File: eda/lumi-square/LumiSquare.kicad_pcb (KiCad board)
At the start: 2 copper layers, 166.5 x 100 mm, 57 parts, among them J1 USB_C_Receptacle_USB2.0_14P, J2 Conn_01x04, J3 Conn_01x04, J4 Conn_01x04, J5 Conn_01x04, J5 USB_C_Receptacle_USB2.0, J6 Conn_01x04, J7 Conn_01x04, Q1 IRLML6244, Q3 IRLML2246, Q4 MMBT3904, Q5 MMBT3904, Q6 MMBT3904, Q7 MMBT3904, U1 MCP73831-2-OT, U2 TPS3840, U3 TLV61070A, U3333333 ATSAMD21J18A-A, U4 TLV61070A, U6 STP16CPC05MTR, U8 MIC5225-3.3YM5

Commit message: - uploading kicad pcb changes
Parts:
- removed J4, J7: Conn_01x04, Connector_PinSocket_2.54mm:PinSocket_1x04_P2.54mm_Vertical
- removed U$1: LOGO-SFE, Button_Pad_Breakout-v05:SFE-NEW-WEBLOGO
- added C11: .001uF, Capacitor_SMD:C_0603_1608Metric_Pad1.08x0.95mm_HandSolder, F.Cu at (175.6, 62.4)
- added C12: .01uF, Capacitor_SMD:C_0603_1608Metric_Pad1.08x0.95mm_HandSolder, F.Cu at (175.6, 64.9)
- added C13: 1uF, Capacitor_THT:CP_Radial_D6.3mm_P2.50mm, F.Cu at (162.6, 65.1)
- added C14: 1uF, Capacitor_THT:CP_Radial_D6.3mm_P2.50mm, F.Cu at (162.6, 73.0)
- added C15: 1uF, Capacitor_THT:CP_Radial_D6.3mm_P2.50mm, F.Cu at (162.6, 80.8)
- added C16: .1uF, Capacitor_SMD:C_1206_3216Metric, F.Cu at (170.6, 62.9)
- added C17: .1uF, Capacitor_SMD:C_1206_3216Metric, F.Cu at (170.6, 66.2)
- added C18: .1uF, Capacitor_SMD:C_1206_3216Metric, F.Cu at (170.6, 69.5)
- added C19: .1uF, Capacitor_SMD:C_1206_3216Metric, F.Cu at (170.6, 72.9)
- added C20: .1uF, Capacitor_SMD:C_1206_3216Metric, F.Cu at (170.6, 76.2)
- added C21: .1uF, Capacitor_SMD:C_1206_3216Metric, F.Cu at (170.6, 79.6)
- added D4: 1N4148W, Diode_SMD:D_SOD-123, F.Cu at (180.7, 62.9)
- added Q2: IRLML2246, Package_TO_SOT_SMD:SOT-23, F.Cu at (156.4, 95.2)
- added Q8: MMBT3904, Package_TO_SOT_SMD:SOT-23, F.Cu at (180.2, 66.8)
- added R11: 220k, Resistor_SMD:R_0603_1608Metric_Pad0.98x0.95mm_HandSolder, F.Cu at (156.1, 98.7)
- added R12: 1k, Resistor_SMD:R_0603_1608Metric_Pad0.98x0.95mm_HandSolder, F.Cu at (175.6, 67.5)
- added R14: 15k, Resistor_SMD:R_0603_1608Metric_Pad0.98x0.95mm_HandSolder, F.Cu at (175.6, 70.0)
- added R15: 15k, Resistor_SMD:R_0603_1608Metric_Pad0.98x0.95mm_HandSolder, F.Cu at (175.6, 72.5)
- added R20: 15k, Resistor_SMD:R_0603_1608Metric_Pad0.98x0.95mm_HandSolder, F.Cu at (175.6, 75.0)
- added R21: 10k, Resistor_SMD:R_0603_1608Metric_Pad0.98x0.95mm_HandSolder, F.Cu at (175.6, 77.5)
- added R22: 2.2k, Resistor_SMD:R_0603_1608Metric_Pad0.98x0.95mm_HandSolder, F.Cu at (175.6, 80.0)
- BT1: moved to B.Cu
- J2, J3: value Conn_01x04 -> Conn_01x12; footprint Connector_PinSocket_2.54mm:PinSocket_1x04_P2.54mm_Vertical -> Connector_PinSocket_2.54mm:PinSocket_1x12_P2.54mm_Vertical
- J5, J6: value Conn_01x04 -> Conn_01x08; footprint Connector_PinSocket_2.54mm:PinSocket_1x04_P2.54mm_Vertical -> Connector_PinSocket_2.54mm:PinSocket_1x08_P2.54mm_Vertical
- R13: value 10k -> 100k
- moved C1 120.6 mm to (164.2, 89.5)
- moved C2 120.6 mm to (164.2, 92.0)
- moved C23234545 120.6 mm to (168.5, 89.5)
- moved C3 120.6 mm to (164.2, 94.5)
- moved C3245345 120.6 mm to (164.2, 104.5)
- moved R1 120.6 mm to (168.5, 92.0)
- moved R11 120.6 mm to (172.8, 94.5)
- moved R12 120.6 mm to (172.8, 97.0)
- moved R13 120.6 mm to (172.8, 99.5)
- moved R2 120.6 mm to (168.5, 94.5)
- moved R3 120.6 mm to (168.5, 97.0)
- moved R4 120.6 mm to (168.5, 99.5)
- moved R5 120.6 mm to (168.5, 102.0)
- moved R6 120.6 mm to (168.5, 104.5)
- moved J5 104.4 mm to (249.5, 116.0)
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- renumbered U3333333 to U5
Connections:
- C3 pad 1: /4.2V Bat -> Net-(Q2-D)
- C4 pad 2: /4.2V Bat -> Net-(Q2-D)
- J2 pad 1: /Matrix Switch 1 -> Net-(J2-Pin_1)
- J3 pad 1: /Matrix Switch 2 -> /Row/Input 1
- J3 pad 2: Net-(J3-Pin_2) -> /Row/Input 2
- J3 pad 3: Net-(J3-Pin_3) -> /Row/Input 3
- J3 pad 4: Net-(J3-Pin_4) -> /Row/Input 4
- J5 pad 1: /Matrix Switch 4 -> +3.3V Main
- J5 pad 2: Net-(J5-Pin_2) -> /MCU TX
- J5 pad 3: Net-(J5-Pin_3) -> /MCU RX
- J5 pad 4: Net-(J5-Pin_4) -> unconnected-(J5-Pin_4-Pad4)
- J6 pad 1: Net-(J6-Pin_1) -> unconnected-(J6-Pin_1-Pad1)
- J6 pad 3: Net-(J6-Pin_3) -> unconnected-(J6-Pin_3-Pad3)
- L1 pad 1: /4.2V Bat -> Net-(Q2-D)
- Q4 pad 2: Net-(J6-Pin_1) -> Net-(J3-Pin_9)
- Q5 pad 2: Net-(J6-Pin_3) -> Net-(J3-Pin_10)
- Q6 pad 2: Net-(J7-Pin_1) -> Net-(J3-Pin_11)
- Q7 pad 2: Net-(J7-Pin_3) -> Net-(J3-Pin_12)
- R16 pad 1: unconnected-(R16-Pad1) -> /LED Col 1
- R17 pad 1: unconnected-(R17-Pad1) -> /LED Col 2
- R18 pad 1: unconnected-(R18-Pad1) -> /LED Col 3
- R19 pad 1: unconnected-(R19-Pad1) -> /LED Col 4
- R6 pad 1: /4.2V Bat -> Net-(Q2-D)
- U2 pad 2: /4.2V Bat -> Net-(Q2-D)
- U3 pad 6: /4.2V Bat -> Net-(Q2-D)
- U5 pad 10: unconnected-(U3333333-PB07-Pad10) -> /Col/Output 4
- U5 pad 11: /Matrix Switch 1 -> /Row/Input 1
- U5 pad 12: /Matrix Switch 2 -> /Row/Input 2
- U5 pad 21: unconnected-(U3333333-VDDIO-Pad21) -> +3.3V Main
- U5 pad 22: Net-(U3333333-GND-Pad22) -> GNDREF
- U5 pad 23: /Matrix Switch 3 -> /Row/Input 3
- U5 pad 24: /Matrix Switch 4 -> /Row/Input 4
- U5 pad 25: unconnected-(U3333333-PB12-Pad25) -> /SPI Dout
- U5 pad 26: unconnected-(U3333333-PB13-Pad26) -> /SPI CLK
- U5 pad 27: unconnected-(U3333333-PB14-Pad27) -> /SPI Latch
- U5 pad 33: Net-(U3333333-GND-Pad22) -> GNDREF
- U5 pad 34: unconnected-(U3333333-VDDIO-Pad34) -> +3.3V Main
- U5 pad 39: unconnected-(U3333333-PB16-Pad39) -> /Previous Btn
- U5 pad 40: unconnected-(U3333333-PB17-Pad40) -> /Next Btn
- U5 pad 41: unconnected-(U3333333-PA20-Pad41) -> /MCU TX
- U5 pad 42: unconnected-(U3333333-PA21-Pad42) -> /MCU RX
- U5 pad 47: Net-(U3333333-GND-Pad22) -> GNDREF
- U5 pad 48: unconnected-(U3333333-VDDIO-Pad48) -> +3.3V Main
- U5 pad 49: unconnected-(U3333333-PB22-Pad49) -> /Difficulty Btn
- U5 pad 5: unconnected-(U3333333-PB04-Pad5) -> /Col/Output 1
- U5 pad 50: unconnected-(U3333333-PB23-Pad50) -> /Buzzer PWM
- U5 pad 52: unconnected-(U3333333-~{RESET}-Pad52) -> /Reset Pin
- U5 pad 54: Net-(U3333333-GND-Pad22) -> GNDREF
- U5 pad 55: unconnected-(U3333333-VDDCORE-Pad55) -> /VDD CORE
- U5 pad 56: unconnected-(U3333333-VDDIN-Pad56) -> +3.3V Main
- U5 pad 57: unconnected-(U3333333-PA30-Pad57) -> /SWCLK
- U5 pad 58: unconnected-(U3333333-PA31-Pad58) -> /SWDIO
- U5 pad 6: unconnected-(U3333333-PB05-Pad6) -> /Col/Output 2
- U5 pad 61: unconnected-(U3333333-PB00-Pad61) -> /LED Col 1
- U5 pad 62: unconnected-(U3333333-PB01-Pad62) -> /LED Col 2
- U5 pad 63: unconnected-(U3333333-PB02-Pad63) -> /LED Col 3
- U5 pad 64: unconnected-(U3333333-PB03-Pad64) -> /LED Col 4
- U5 pad 7: unconnected-(U3333333-GNDANA-Pad7) -> GNDREF
- U5 pad 8: unconnected-(U3333333-VDDANA-Pad8) -> +3.3V Main
- U5 pad 9: unconnected-(U3333333-PB06-Pad9) -> /Col/Output 3
- U6 pad 10: Net-(J3-Pin_4) -> Net-(J2-Pin_6)
- U6 pad 11: Net-(J4-Pin_2) -> Net-(J2-Pin_7)
- U6 pad 12: Net-(J4-Pin_3) -> Net-(J2-Pin_8)
- U6 pad 13: Net-(J4-Pin_4) -> Net-(J2-Pin_9)
- U6 pad 14: Net-(J5-Pin_2) -> Net-(J2-Pin_10)
- U6 pad 15: Net-(J5-Pin_3) -> Net-(J2-Pin_11)
- U6 pad 16: Net-(J5-Pin_4) -> Net-(J2-Pin_12)
- U6 pad 2: unconnected-(U6-SIN-Pad2) -> /SPI Dout
- U6 pad 21: unconnected-(U6-BLANK-Pad21) -> GNDREF
- U6 pad 23: unconnected-(U6-RSET-Pad23) -> Net-(U6-RSET)
- U6 pad 3: unconnected-(U6-CLK-Pad3) -> /SPI CLK
- U6 pad 4: unconnected-(U6-LATCH-Pad4) -> /SPI Latch
- U6 pad 5: Net-(J2-Pin_2) -> Net-(J2-Pin_1)
- U6 pad 6: Net-(J2-Pin_3) -> Net-(J2-Pin_2)
- U6 pad 7: Net-(J2-Pin_4) -> Net-(J2-Pin_3)
- U6 pad 8: Net-(J3-Pin_2) -> Net-(J2-Pin_4)
- U6 pad 9: Net-(J3-Pin_3) -> Net-(J2-Pin_5)
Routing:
- net /5V USB: track 16.1 -> 6.01 mm
- net unconnected-(J1-SHIELD-PadS1): track 0.00 -> 10.1 mm
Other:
- board size 166.5 x 100 mm -> 87.2 x 87.2 mm

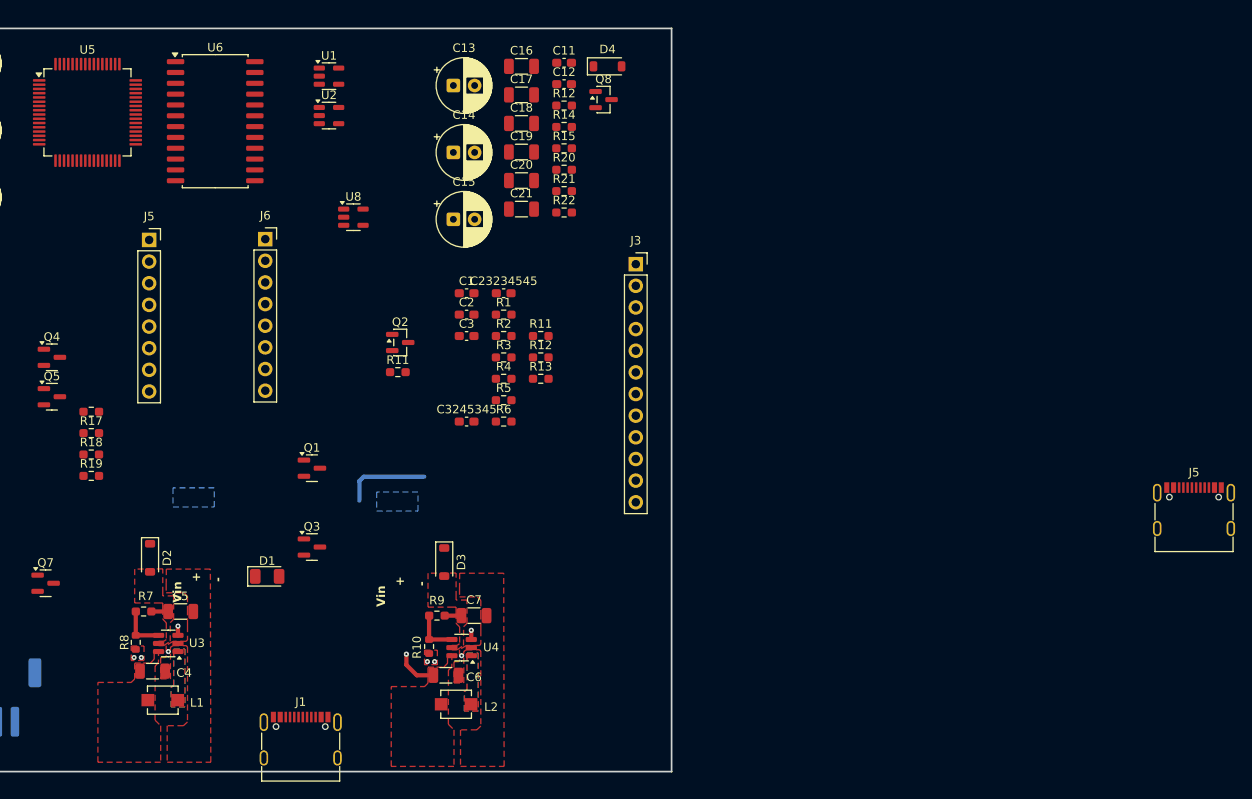
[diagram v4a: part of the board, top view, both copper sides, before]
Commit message: -Added circuity for esd on usb. - Add p chanel mosfets. - added new footprint, symbol, and step files
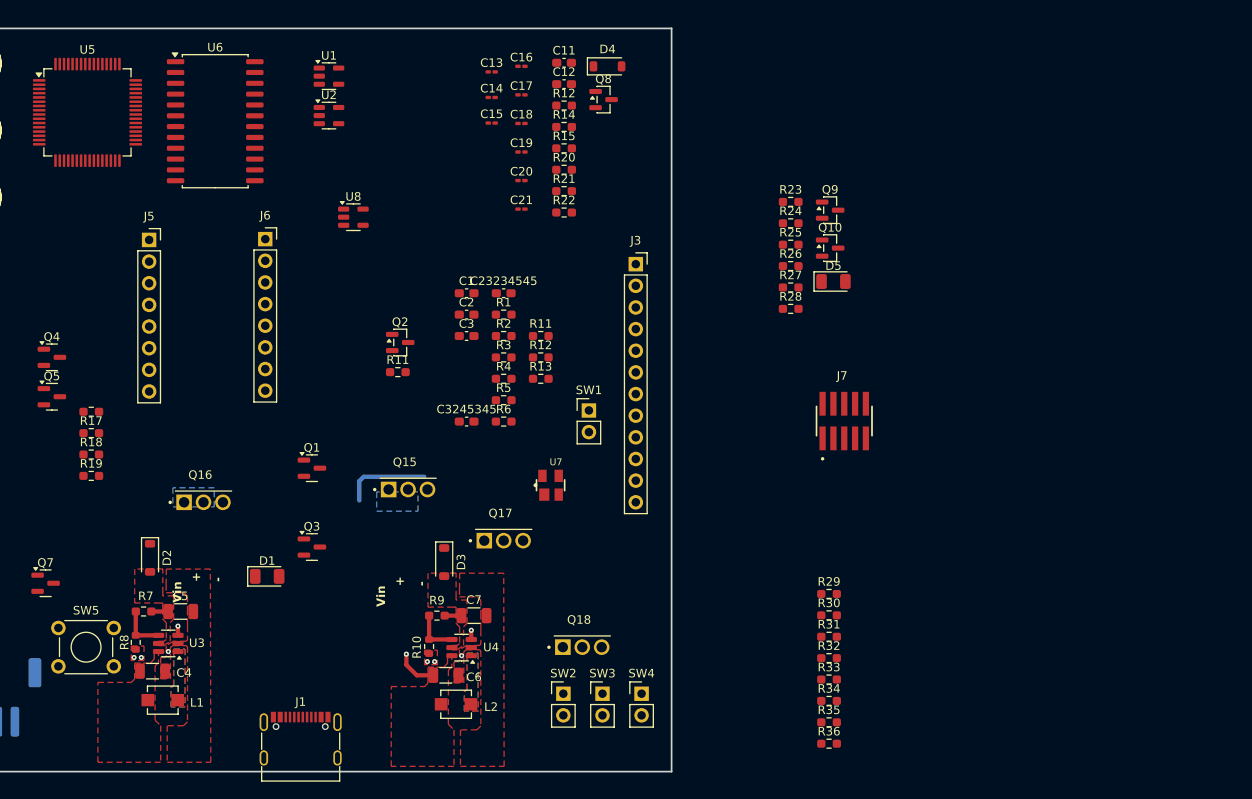
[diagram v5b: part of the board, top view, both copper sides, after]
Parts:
- removed the J5 at (249.5, 116.0)
- added D5: LED, LED_SMD:LED_1206_3216Metric, F.Cu at (207.2, 88.1)
- added J7: FTSH-105-01-X-DV-P-K-X, FTSH-105-01-X-DV-P-K-X:SAMTEC_FTSH-105-01-X-DV-P-K-X, F.Cu at (208.5, 104.5)
- added Q10: IRLML2246, Package_TO_SOT_SMD:SOT-23, F.Cu at (206.8, 84.2)
- added Q15: TSM680P06CH, TSM680P06CH:TO228P680X245X847-3, F.Cu at (157.3, 112.5)
- added Q16: TSM680P06CH, TSM680P06CH:TO228P680X245X847-3, F.Cu at (133.3, 114.0)
- added Q17: TSM680P06CH, TSM680P06CH:TO228P680X245X847-3, F.Cu at (168.5, 118.5)
- added Q18: TSM680P06CH, TSM680P06CH:TO228P680X245X847-3, F.Cu at (177.7, 131.0)
- added Q9: MMBT3904, Package_TO_SOT_SMD:SOT-23, F.Cu at (206.8, 79.7)
- added R23: 330, Resistor_SMD:R_0603_1608Metric_Pad0.98x0.95mm_HandSolder, F.Cu at (202.2, 78.8)
- added R24: 1.3k, Resistor_SMD:R_0603_1608Metric_Pad0.98x0.95mm_HandSolder, F.Cu at (202.2, 81.3)
- added R25: 1.3k, Resistor_SMD:R_0603_1608Metric_Pad0.98x0.95mm_HandSolder, F.Cu at (202.2, 83.8)
- added R26: 33k, Resistor_SMD:R_0603_1608Metric_Pad0.98x0.95mm_HandSolder, F.Cu at (202.2, 86.3)
- added R27: 41k, Resistor_SMD:R_0603_1608Metric_Pad0.98x0.95mm_HandSolder, F.Cu at (202.2, 88.8)
- added R28: 100k, Resistor_SMD:R_0603_1608Metric_Pad0.98x0.95mm_HandSolder, F.Cu at (202.2, 91.3)
- added R29: 100k, Resistor_SMD:R_0603_1608Metric_Pad0.98x0.95mm_HandSolder, F.Cu at (206.7, 124.8)
- added R30: 47k, Resistor_SMD:R_0603_1608Metric_Pad0.98x0.95mm_HandSolder, F.Cu at (206.7, 127.3)
- added R31: 100k, Resistor_SMD:R_0603_1608Metric_Pad0.98x0.95mm_HandSolder, F.Cu at (206.7, 129.8)
- added R32: 47k, Resistor_SMD:R_0603_1608Metric_Pad0.98x0.95mm_HandSolder, F.Cu at (206.7, 132.3)
- added R33: 100k, Resistor_SMD:R_0603_1608Metric_Pad0.98x0.95mm_HandSolder, F.Cu at (206.7, 134.8)
- added R34: 47k, Resistor_SMD:R_0603_1608Metric_Pad0.98x0.95mm_HandSolder, F.Cu at (206.7, 137.3)
- added R35: 100k, Resistor_SMD:R_0603_1608Metric_Pad0.98x0.95mm_HandSolder, F.Cu at (206.7, 139.8)
- added R36: 47k, Resistor_SMD:R_0603_1608Metric_Pad0.98x0.95mm_HandSolder, F.Cu at (206.7, 142.3)
- added SW1: SW_SPST, Connector_PinHeader_2.54mm:PinHeader_1x02_P2.54mm_Vertical, F.Cu at (178.5, 103.2)
- added SW2: SW_Push, Connector_PinHeader_2.54mm:PinHeader_1x02_P2.54mm_Vertical, F.Cu at (175.5, 136.5)
- added SW3: SW_Push, Connector_PinHeader_2.54mm:PinHeader_1x02_P2.54mm_Vertical, F.Cu at (180.1, 136.5)
- added SW4: SW_Push, Connector_PinHeader_2.54mm:PinHeader_1x02_P2.54mm_Vertical, F.Cu at (184.7, 136.5)
- added SW5: SW_Push, Button_Switch_THT:SW_TH_Tactile_Omron_B3F-100x, F.Cu at (116.2, 128.8)
- added U7: CM1224-02SR, CM1224-02SR:SOT143, F.Cu at (174.0, 112.0)
- C13, C14, C15: footprint Capacitor_THT:CP_Radial_D6.3mm_P2.50mm -> Capacitor_SMD:C_0201_0603Metric_Pad0.64x0.40mm_HandSolder
- C16, C17, C18, C19, C20, C21: footprint Capacitor_SMD:C_1206_3216Metric -> Capacitor_SMD:C_0201_0603Metric_Pad0.64x0.40mm_HandSolder
- R12: value 1k -> 200
- moved C15 12.2 mm to (167.1, 69.5)
- moved C14 7.86 mm to (167.1, 66.5)
- moved C13 4.78 mm to (167.1, 63.5)
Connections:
- J1 pad A6: unconnected-(J1-D+-PadA6) -> /TARGET USB P
- J1 pad A7: unconnected-(J1-D--PadA7) -> /TARGET USB N
- J1 pad B6: unconnected-(J1-D+-PadB6) -> /TARGET USB P
- J1 pad B7: unconnected-(J1-D--PadB7) -> /TARGET USB N
- J3 pad 10: Net-(J3-Pin_10) -> /Col 2 Anode
- J3 pad 11: Net-(J3-Pin_11) -> /Col 3 Anode
- J3 pad 12: Net-(J3-Pin_12) -> /Col 4 Anode
- J3 pad 9: Net-(J3-Pin_9) -> /Col 1 Anode
- Q4 pad 2: Net-(J3-Pin_9) -> GNDREF
- Q4 pad 3: /5.3V Out -> Net-(Q4-C)
- Q5 pad 2: Net-(J3-Pin_10) -> GNDREF
- Q5 pad 3: /5.3V Out -> Net-(Q5-C)
- Q6 pad 2: Net-(J3-Pin_11) -> GNDREF
- Q6 pad 3: /5.3V Out -> Net-(Q6-C)
- Q7 pad 2: Net-(J3-Pin_12) -> GNDREF
- Q7 pad 3: /5.3V Out -> Net-(Q7-C)
- U5 pad 31: unconnected-(U5-PA14-Pad31) -> /PA14 USB VBUS
- U5 pad 45: unconnected-(U5-PA24-Pad45) -> /TARGET USB N
- U5 pad 46: unconnected-(U5-PA25-Pad46) -> /TARGET USB P

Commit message: Adding updateds to pcb and schematic design
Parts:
- removed J5, J6: Conn_01x08, Connector_PinSocket_2.54mm:PinSocket_1x08_P2.54mm_Vertical
- removed the R11 at (172.8, 94.5)
- added BZ2: RDT-4.000-1375-NS1, RDT.pretty:RDT-4.000-1375-NS1, F.Cu at (111.0, 135.5)
- added U9: DFR0299, DFR0299:MODULE_DFR0299, F.Cu at (116.5, 70.5)
- C13, C14, C15, C16, C17, C18, C19, C20, C21: footprint Capacitor_SMD:C_0201_0603Metric_Pad0.64x0.40mm_HandSolder -> Capacitor_SMD:C_0603_1608Metric_Pad1.08x0.95mm_HandSolder
- SW5, U6: moved to B.Cu
- moved C1 85.5 mm to (249.6, 86.5)
- moved C23234545 85.5 mm to (253.9, 86.5)
- moved C3245345 85.5 mm to (249.6, 101.5)
- moved R1 85.5 mm to (253.9, 89.0)
- moved R12 85.5 mm to (258.3, 94.0)
- moved R13 85.5 mm to (258.3, 96.5)
- moved R2 85.5 mm to (253.9, 91.5)
- moved R3 85.5 mm to (253.9, 94.0)
- moved R4 85.5 mm to (253.9, 96.5)
- moved J7 75.6 mm to (144.6, 64.0)
- moved R30 74.0 mm to (146.3, 84.5), turned to 180 degrees
- moved R34 72.3 mm to (146.3, 97.5), turned to 180 degrees
- moved C10 72.2 mm to (168.5, 112.5)
- moved D1 70.3 mm to (71.2, 112.0)
- moved C9 69.9 mm to (160.8, 112.5)
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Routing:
- net /Col 1 Anode: track 0.00 -> 56.1 mm
- net /Col 3 Anode: track 0.00 -> 47.9 mm
- net /Col 2 Anode: track 0.00 -> 34.2 mm
- net /5V USB: track 6.01 -> 33.3 mm, vias 2 -> 4
- net /Col 4 Anode: track 0.00 -> 26.5 mm
- net GNDREF: track 0.00 -> 24.0 mm, vias 6 -> 23
- net unconnected-(J1-SHIELD-PadS1): track 10.1 -> 0.00 mm
- net Net-(Q7-B): track 0.00 -> 8.21 mm
- net Net-(Q5-B): track 0.00 -> 8.21 mm
- net Net-(Q6-B): track 0.00 -> 7.87 mm
- net Net-(Q4-B): track 0.00 -> 7.87 mm
- net Net-(Q6-C): track 0.00 -> 7.28 mm
- net Net-(Q7-C): track 0.00 -> 7.06 mm
- net Net-(Q4-C): track 0.00 -> 6.75 mm
- net Net-(Q5-C): track 0.00 -> 6.56 mm
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- added copper zone on F.Cu, net /5.3V Out
- added copper zone on F.Cu, net Net-(Q2-D)
- added copper zone on B.Cu, net Net-(U3-SW)
- added copper zone on F.Cu, net Net-(U3-SW)
- added copper zone on B.Cu, net Net-(U4-SW)
- added copper zone on F.Cu, net Net-(U4-SW)
- removed copper zone on B.Cu, net (none)
- removed copper zone on F.Cu, net (none)
- removed copper zone on F.Cu, net /4.2V Bat
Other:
- board text removed: "+"
- board text removed: "-"
- board text removed: "Vin"

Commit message: Made more progress with the pcb layout
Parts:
- removed C23234545: 1uF, Capacitor_SMD:C_0603_1608Metric_Pad1.08x0.95mm_HandSolder
- removed C3245345: 2.2uF, Capacitor_SMD:C_0603_1608Metric_Pad1.08x0.95mm_HandSolder
- removed the R12 at (258.3, 94.0)
- added C22: 1uF, Capacitor_SMD:C_0603_1608Metric_Pad1.08x0.95mm_HandSolder, F.Cu at (169.5, 73.1)
- added C23: 2.2uF, Capacitor_SMD:C_0603_1608Metric_Pad1.08x0.95mm_HandSolder, F.Cu at (159.5, 73.1)
- added J4: Conn_01x02, Connector_JST:JST_SH_BM02B-SRSS-TB_1x02-1MP_P1.00mm_Vertical, F.Cu at (88.3, 66.7)
- added REF**: M2, MountingHole:MountingHole_2.2mm_M2_DIN965_Pad, F.Cu at (104.5, 142.1)
- added REF**: M2, MountingHole:MountingHole_2.2mm_M2_DIN965_Pad, F.Cu at (104.5, 61.9)
- added REF**: M2, MountingHole:MountingHole_2.2mm_M2_DIN965_Pad, F.Cu at (185.0, 61.6)
- added REF**: M2, MountingHole:MountingHole_2.2mm_M2_DIN965_Pad, F.Cu at (185.0, 142.4)
- C16, C17, C18, C19, C2, C20, U5: moved to B.Cu
- D1, D5: footprint LED_SMD:LED_1206_3216Metric -> Connector_JST:JST_SH_BM02B-SRSS-TB_1x02-1MP_P1.00mm_Vertical
- SW1, SW2, SW3, SW4: footprint Connector_PinHeader_2.54mm:PinHeader_1x02_P2.54mm_Vertical -> Connector_JST:JST_SH_BM02B-SRSS-TB_1x02-1MP_P1.00mm_Vertical
- SW5: footprint Button_Switch_THT:SW_TH_Tactile_Omron_B3F-100x -> Button_Switch_SMD:SW_SPST_TL3342
- U6: moved to F.Cu
- moved D4 145.6 mm to (127.5, 132.0), turned to 90 degrees
- moved Q8 138.8 mm to (127.5, 123.9), turned to -90 degrees
- moved C19 133.0 mm to (112.5, 105.0), turned to -90 degrees
- moved C16 126.8 mm to (119.5, 96.0), turned to 180 degrees
- moved C18 126.6 mm to (124.9, 114.0), turned to 180 degrees
- moved R22 124.9 mm to (128.4, 117.5), turned to -90 degrees
- moved R2 118.4 mm to (143.4, 134.0), turned to 90 degrees
- moved C17 118.2 mm to (127.5, 96.0)
- moved R1 116.5 mm to (146.4, 134.0), turned to 90 degrees
- moved R12 112.4 mm to (135.0, 86.9)
- moved C1 112.2 mm to (152.0, 142.0), turned to -90 degrees
- moved C20 112.0 mm to (134.0, 105.8), turned to -90 degrees
- moved R3 109.9 mm to (155.0, 141.9), turned to 90 degrees
- moved C21 109.5 mm to (129.5, 83.5)
- moved U1 105.7 mm to (159.5, 140.8), turned to 180 degrees
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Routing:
- net Net-(J2-Pin_12): track 0.00 -> 52.9 mm
- net Net-(J2-Pin_11): track 0.00 -> 46.9 mm
- net Net-(J2-Pin_10): track 0.00 -> 41.1 mm
- net Net-(J2-Pin_9): track 0.00 -> 35.7 mm
- net GNDREF: track 24.0 -> 57.7 mm, vias 23 -> 38
- net /5V USB: track 33.3 -> 1.08 mm, vias 4 -> 1
- net +3.3V Main: track 0.00 -> 24.0 mm, vias 0 -> 2
- net Net-(Q1-D): track 4.67 -> 24.7 mm, vias 0 -> 3
- net Net-(Q3-G): track 0.00 -> 17.1 mm, vias 0 -> 2
- net Net-(J2-Pin_1): track 0.00 -> 17.0 mm
- net Net-(BZ2--): track 0.00 -> 16.7 mm
- net Net-(J2-Pin_8): track 0.00 -> 16.4 mm
- net Net-(J2-Pin_2): track 0.00 -> 16.4 mm
- net Net-(J2-Pin_3): track 0.00 -> 15.9 mm
- net Net-(J2-Pin_7): track 0.00 -> 15.9 mm
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- added copper zone on F.Cu, net +3.3V Main

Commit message: Made more progress on the pcb
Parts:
- C13, C14, C15, C21, R14, R15, R20, R21: moved to B.Cu
- moved C11 123.9 mm to (123.5, 83.5)
- moved C12 117.5 mm to (129.5, 83.5)
- moved R21 110.5 mm to (136.4, 95.0), turned to 180 degrees
- moved R14 86.7 mm to (157.0, 70.5), turned to -90 degrees
- moved C13 83.6 mm to (153.0, 70.5), turned to 90 degrees
- moved R15 79.2 mm to (164.2, 70.5), turned to -90 degrees
- moved C14 75.6 mm to (160.5, 70.5), turned to 90 degrees
- moved R20 71.6 mm to (171.5, 70.5), turned to -90 degrees
- moved C15 67.6 mm to (168.0, 70.5), turned to 90 degrees
- moved J4 20.0 mm to (105.5, 77.0), turned to 90 degrees
- moved C19 18.1 mm to (127.9, 95.5), turned to 90 degrees
- moved C16 16.7 mm to (135.5, 100.8), turned to 90 degrees
- moved C17 15.1 mm to (135.5, 108.8), turned to -90 degrees
- moved C21 14.8 mm to (120.9, 95.5), turned to 90 degrees
- moved C20 14.0 mm to (124.4, 116.0)
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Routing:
- net /Row/Input 4: track 0.00 -> 161.9 mm, vias 0 -> 1
- net /Row/Input 3: track 0.00 -> 149.9 mm, vias 0 -> 1
- net /Row/Input 2: track 0.00 -> 123.8 mm, vias 0 -> 1
- net /Row/Input 1: track 0.00 -> 110.4 mm, vias 0 -> 1
- net /Reset Pin: track 0.00 -> 90.9 mm
- net /Col/Output 3: track 0.00 -> 80.0 mm, vias 0 -> 1
- net /Col/Output 4: track 0.00 -> 78.7 mm, vias 0 -> 1
- net /Col/Output 2: track 0.00 -> 69.4 mm, vias 0 -> 1
- net /Col/Output 1: track 0.00 -> 69.2 mm, vias 0 -> 1
- net /Difficulty Btn: track 0.00 -> 61.8 mm
- net /LED Col 2: track 0.00 -> 53.7 mm, vias 0 -> 1
- net /Next Btn: track 0.00 -> 49.2 mm
- net /Previous Btn: track 0.00 -> 41.6 mm
- net /LED Col 4: track 0.00 -> 41.3 mm, vias 0 -> 1
- net /LED Col 1: track 0.00 -> 40.0 mm, vias 0 -> 1
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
